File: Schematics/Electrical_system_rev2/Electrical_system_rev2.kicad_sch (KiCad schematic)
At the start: 38 parts, among them J1 DTM04-12PA-L012, J10 DTM06-12SA, J13 DTM06-12SA, J14 DTM04-12PA-L012, J17 DTM06-12SA, J18 DTM04-12PA-L012, J19 211102-1, J2 DTM06-12SA, J20 206429-1, J21 211102-1, J22 206429-1, J23 206429-1, J24 211102-1, J7 UPCR012ALS1, J8 UPCP012ALS2, SW3 2843011, SW4 2843011, SW5 84-5330.0020, SW7 84-5330.0020

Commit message: fixed checkbox
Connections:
- net SDC_to_TSMS: no longer J23.4 (Pin_4)
- net SDC_to_dash: now also J23.4 (Pin_4); no longer J23.2 (Pin_2)
- net at J24.2 (Pin_2): no longer SW7.1 (A)
- net at J24.3 (Pin_3): no longer SW5.1 (A)
- net at J2.9 (Pin_9): no longer J2.9 (Pin_9)
- net Checkbox/Reset_out: no longer names the net of J1.12 (Pin_12)
- net Checkbox/SDC1: no longer names the net of J1.9 (Pin_9)
- net SDC_from_dash: no longer names the net of J23.3 (Pin_3)
- new net: SW5.1 (A), SW7.1 (A)
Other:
- sheet Checkbox ports: added none; removed Reset_out, SDC1
- sheet Dashboard ports: added SDC_to_TSMS; removed SDC_from_dash

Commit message: SDC
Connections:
- net SDC_to_SDB: now also J14.2 (Pin_2); no longer J14.4 (Pin_4), SW4.1 (A)
- net Checkbox/SDC3: now reaches J13.2 (Pin_2)
- net Checkbox/GLV_switch renamed Checkbox/GLVMS_in
- new net: J14.4 (Pin_4), SW4.1 (A)
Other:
- sheet Checkbox ports: added GLVMS_in, Reset_out, SDC3, fan1-, fan2-, pump2-; removed GLV_switch
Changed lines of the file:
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@@
 	)
 	(junction
-		(at 288.29 210.82)
-		(diameter 0)
-		(color 0 0 0 0)
-	)
-	(junction
 		(at 300.99 210.82)
 		(diameter 0)
@@
 		)
 	)
+	(wire
+		(pts
+			(xy 306.07 170.18) (xy 306.07 175.26)
+		)
+		(stroke
+			(width 0)
+			(type default)
+		)
+	)
 	(bus
 		(pts
@@
 		)
 	)
-	(wire
+	(bus
 		(pts
-			(xy 284.48 210.82) (xy 288.29 210.82)
+			(xy 313.69 151.13) (xy 316.23 151.13)
 		)
 		(stroke
@@
 		)
 	)
-	(bus
+	(wire
 		(pts
-			(xy 313.69 151.13) (xy 316.23 151.13)
+			(xy 289.56 173.99) (xy 289.56 162.56)
 		)
 		(stroke
 			(width 0)
 			(type default)
+			(color 204 102 0 1)
 		)
 	)
 	(wire
 		(pts
-			(xy 289.56 173.99) (xy 289.56 162.56)
+			(xy 306.07 148.59) (xy 306.07 154.94)
 		)
 		(stroke
 			(width 0)
 			(type default)
-			(color 204 102 0 1)
 		)
 	)
@@
 		)
 	)
-	(global_label "SIN1"
-		(shape bidirectional)
-		(at 271.78 323.85 270)
+	(global_label "SDC_to_SDB"
+		(shape output)
+		(at 306.07 175.26 270)
 		(fields_autoplaced yes)
 		(effects
@@
 		)
 		(property "Intersheetrefs" "${INTERSHEET_REFS}"
-			(at 271.78 332.2214 90)
+			(at 306.07 189.5541 90)
 			(effects
 				(font
@@
 		)
 	)
-	(global_label "TEMP_sig"
+	(global_label "SIN1"
 		(shape bidirectional)
-		(at 259.08 323.85 270)
+		(at 271.78 323.85 270)
 		(fields_autoplaced yes)
 		(effects
@@
 		)
 		(property "Intersheetrefs" "${INTERSHEET_REFS}"
-			(at 259.08 336.4546 90)
+			(at 271.78 332.2214 90)
 			(effects
 				(font
@@
 		)
 	)
-	(global_label "COS2"
+	(global_label "TEMP_sig"
 		(shape bidirectional)
-		(at 394.97 299.72 0)
+		(at 259.08 323.85 270)
 		(fields_autoplaced yes)
 		(effects
@@
 				(size 1.27 1.27)
 			)
-			(justify left)
+			(justify right)
 		)
 		(property "Intersheetrefs" "${INTERSHEET_REFS}"
-			(at 404.0066 299.72 0)
+			(at 259.08 336.4546 90)
 			(effects
 				(font
 					(size 1.27 1.27)
 				)
-				(justify left)
+				(justify right)
 				(hide yes)
 			)
 		)
 	)
-	(global_label "SDC_to_SDB"
-		(shape input)
-		(at 360.68 233.68 90)
+	(global_label "COS2"
+		(shape bidirectional)
+		(at 394.97 299.72 0)
 		(fields_autoplaced yes)
 		(effects
@@
 		)
 		(property "Intersheetrefs" "${INTERSHEET_REFS}"
-			(at 360.68 219.3859 90)
+			(at 404.0066 299.72 0)
 			(effects
 				(font
@@
 	)
 	(global_label "SDC_to_SDB"
-		(shape output)
-		(at 284.48 210.82 180)
+		(shape input)
+		(at 360.68 233.68 90)
 		(fields_autoplaced yes)
 		(effects
@@
 				(size 1.27 1.27)
 			)
-			(justify right)
+			(justify left)
 		)
 		(property "Intersheetrefs" "${INTERSHEET_REFS}"
-			(at 270.1859 210.82 0)
+			(at 360.68 219.3859 90)
 			(effects
 				(font
 					(size 1.27 1.27)
 				)
-				(justify right)
+				(justify left)
 				(hide yes)
 			)
@@
 			)
 		)
-		(pin "GLV_switch" input
+		(pin "GLVMS_in" input
 			(at 311.15 148.59 270)
 			(effects
@@
 			(effects
 				(font
+					(size 1.27 1.27)
+				)
+				(justify left)
+			)
+		)
+		(pin "SDC3" input
+			(at 306.07 148.59 270)
+			(effects
+				(font
+					(size 1.27 1.27)
+				)
+				(justify left)
+			)
+		)
+		(pin "fan1-" input
+			(at 288.29 148.59 270)
+			(effects
+				(font
+					(size 1.27 1.27)
+				)
+				(justify left)
+			)
+		)
+		(pin "fan2-" input
+			(at 284.48 148.59 270)
+			(effects
+				(font
+					(size 1.27 1.27)
+				)
+				(justify left)
+			)
+		)
+		(pin "Reset_out" input
+			(at 299.72 148.59 270)
+			(effects
+				(font
+					(size 1.27 1.27)
+				)
+				(justify left)
+			)
+		)
+		(pin "pump2-" input
+			(at 295.91 148.59 270)
+			(effects
+				(font

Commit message: updating of electrical system
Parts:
- removed J7 (x2): UPCR012ALS1, symbol Connector:Conn_01x04_Socket
- removed J8 (x2): UPCP012ALS2, symbol Connector:Conn_01x04_Pin
- added J25: DTM04-12PA-L012, symbol Connector:Conn_01x12_Socket
- added J26: DTM06-12SA, symbol Connector:Conn_01x12_Pin
- added J27: UPCP012ALS2, symbol Connector:Conn_01x04_Pin
- added J28: UPCR012ALS1, symbol Connector:Conn_01x04_Socket
- added J29: 33482-4001, symbol Connector:Conn_01x04_Socket
- added SW10: 2843011, symbol Switch:SW_SPST
- added U18: ~, symbol FSAE:Emeter
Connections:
- net Checkbox/GLV+_fan2 is gone; now on an unnamed net: J17.2 (Pin_2)
- net Checkbox/HV+: now also J21.1 (Pin_1)
- net Checkbox/HV-: now also J21.2 (Pin_2)
- net SDC_to_TSMS: now also J26.1 (Pin_1); no longer SW3.1 (A)
- net at J8.3 (Pin_3): now also B1. (Battery-)
- net at J8.4 (Pin_4): now also J27.3 (Pin_3)
- net at B1. (Battery-): now also J27.4 (Pin_4)
- net at J14.1 (Pin_1): now also SW10.2 (B); no longer D4.2 (A)
- net at SW3.2 (B): now also J25.1 (Pin_1); no longer J14.3 (Pin_3)
- net at J14.4 (Pin_4): now also J26.3 (Pin_3); no longer SW4.1 (A)
- net TSMS_to_accum: now reaches J2.9 (Pin_9)
- net TSMS_to_accum: now also J14.3 (Pin_3), J26.2 (Pin_2)
- net HV+: now reaches R3.2, TP2.1
- net HV+: now also U18. (VSENSE)
- net Checkbox/GLV+_fan1: no longer names the net of J17.1 (Pin_1)
- net Checkbox/GLV+_pump1: no longer names the net of J17.5 (Pin_5), J17.6 (Pin_6)
- net Checkbox/GLV+_pump2: no longer names the net of J17.3 (Pin_3), J17.4 (Pin_4)
- net Checkbox/accum_motor+: no longer names the net of J17.7 (Pin_7)
- net Checkbox/accum_motor-: no longer names the net of J17.8 (Pin_8)
- net Checkbox/temp1_motor+: no longer names the net of J17.11 (Pin_11)
- net Checkbox/temp1_motor-: no longer names the net of J17.12 (Pin_12)
- net Checkbox/temp2_motor+: no longer names the net of J17.9 (Pin_9)
- net Checkbox/temp2_motor-: no longer names the net of J17.10 (Pin_10)
- new net: J25.3 (Pin_3), SW4.2 (B)
- new net: J14.5 (Pin_5), J26.4 (Pin_4)
- new net: J29.1 (Pin_1), U18.4 (CANH)
- new net: J29.2 (Pin_2), U18.3 (CANL)
- new net: D4.2 (A), SW10.1 (A)
- new net: J28.3 (Pin_3), U18. (VSENSE)
- new net: J28.4 (Pin_4), U18. (VSENSE)
- new net GLVMS: J25.4 (Pin_4), J29.4 (Pin_4), SW4.1 (A), U18.1 (GLV+)
- new net GND: J25.5 (Pin_5), J29.3 (Pin_3), TP3.1, U18.2 (GLV-)
- new net GNDPWR: J26.5 (Pin_5)
- new net TSMS: J28.1 (Pin_1), SW3.1 (A)
- new net TSMS_out: J25.2 (Pin_2), J28.2 (Pin_2)
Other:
- sheet Checkbox ports: added GLV+_fan, GLV+_pump_accum, GLV+_pump_motor; removed GLV+_fan1, GLV+_fan2, GLV+_pump1, GLV+_pump2, HV+_to_motor, HV-_to_motor, accum_motor+, accum_motor-, fan1-, fan2-, temp1_motor+, temp1_motor-, temp2_motor+, temp2_motor-
- sheet Cooling ports: added Fans-, GLV+_fan, GLV+_pump_accum, GLV+_pump_motor, Pump_accum-, pump_motor_pwm, temp1+, temp1-, temp2+, temp2-; removed GLV+_pump1, fan1+, fan2+, pump1_control, pump2_control, temp1_motor+, temp1_motor-, temp2_motor+, temp2_motor-
- sheet Dashboard ports: added Fans-, Pump_accum-, temp1+, temp1-, temp2+, temp2-, temp_accum+, temp_accum-; removed Reset_from_dash
- note added: "Brake switch"
- note added: "Download Connector"
- note added: "GND while charging, floating when not"
- note added: "HV High Current"
- note added: "HV Low Current"
- note added: "HVD"
- note added: "LV"
- note removed: "GND while charging, 12V when not"
- moved on the sheet: J19, J22, R2, R3, TP1, TP2

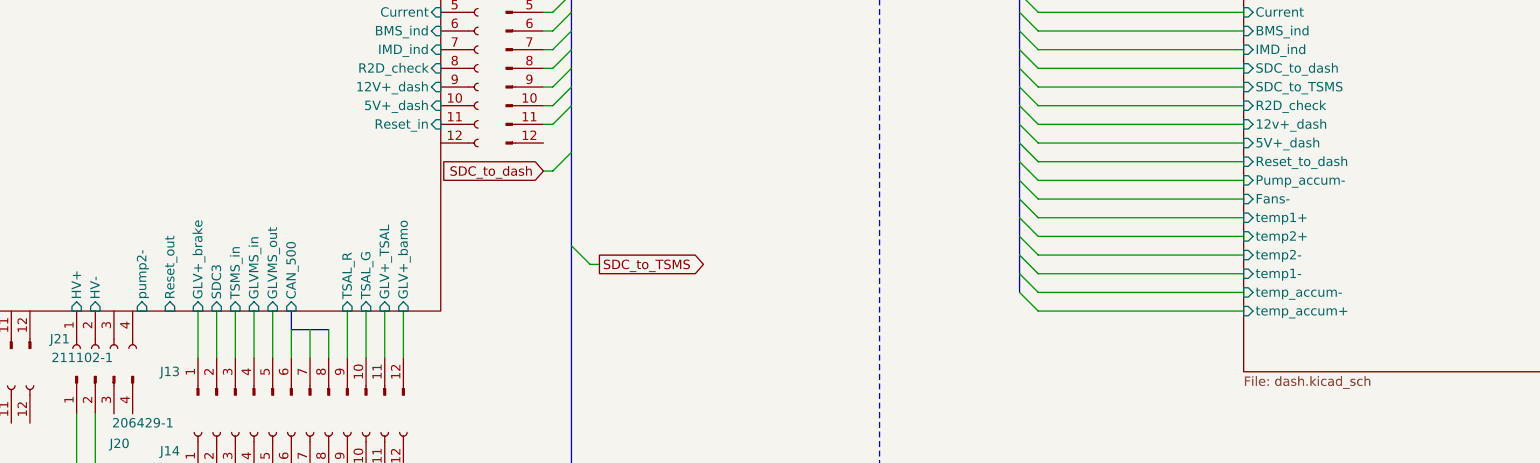
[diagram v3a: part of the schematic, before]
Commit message: fixed reset switch
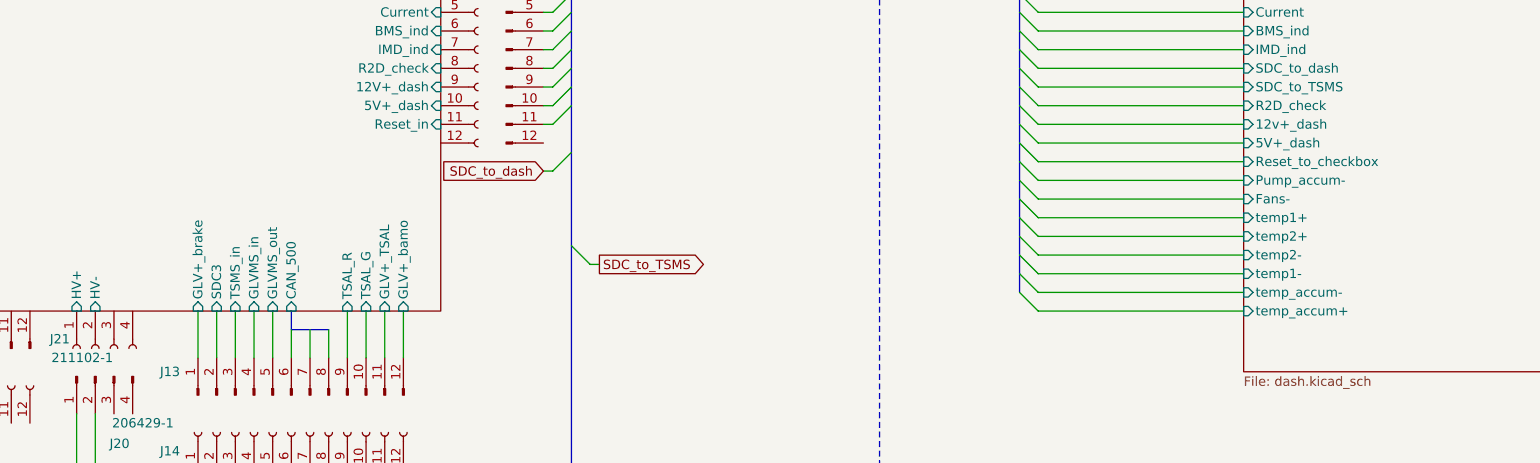
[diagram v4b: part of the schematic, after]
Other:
- sheet Checkbox ports: added none; removed Reset_out, pump2-
- sheet Dashboard ports: added Reset_to_checkbox; removed Reset_to_dash
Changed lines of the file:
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@@
-			)
-		)
-		(pin "Reset_out" input
-			(at 299.72 148.59 270)
-			(effects
-				(font
-					(size 1.27 1.27)
-				)
-				(justify left)
-			)
-		)
-		(pin "pump2-" input
-			(at 295.91 148.59 270)
-			(effects
-				(font
-					(size 1.27 1.27)
-				)
-				(justify left)
 			)
 		)
@@
 			)
 		)
-		(pin "Reset_to_dash" input
+		(pin "Reset_to_checkbox" input
 			(at 445.77 128.27 180)
 			(effects

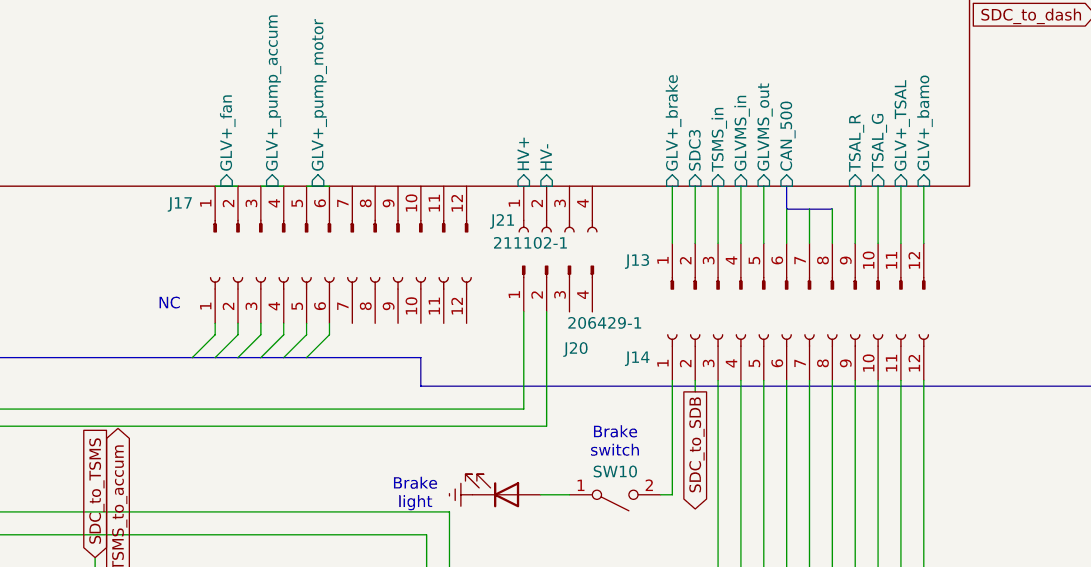
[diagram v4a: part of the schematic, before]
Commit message: swapped male and female connectors
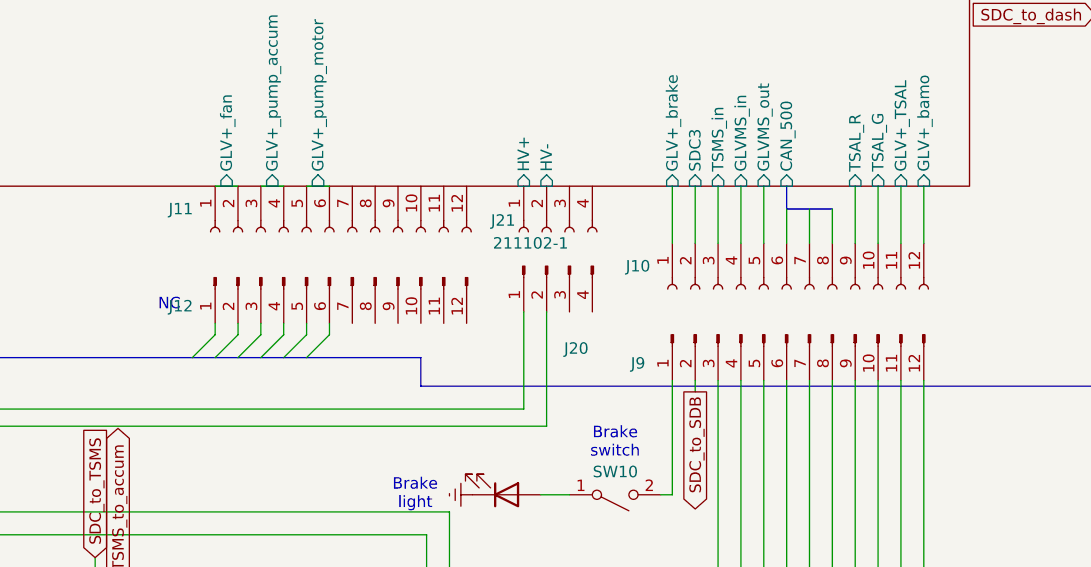
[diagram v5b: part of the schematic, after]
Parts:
- removed J13, J17: DTM06-12SA, symbol Connector:Conn_01x12_Pin
- removed J14, J18: DTM04-12PA-L012, symbol Connector:Conn_01x12_Socket
- added J10, J11: DTM04-12PA-L012, symbol Connector:Conn_01x12_Socket
- added J12, J9: DTM06-12SA, symbol Connector:Conn_01x12_Pin
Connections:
- net Checkbox/GLV+_TSAL: now also J10.11 (Pin_11)
- net Checkbox/GLV+_bamo: now also J10.12 (Pin_12)
- net Checkbox/GLV+_brake: now also J10.1 (Pin_1)
- net Checkbox/GLVMS_in: now also J10.4 (Pin_4)
- net Checkbox/GLVMS_out: now also J10.5 (Pin_5)
- net Checkbox/SDC3: now also J10.2 (Pin_2)
- net Checkbox/TSAL_G: now also J10.10 (Pin_10)
- net Checkbox/TSAL_R: now also J10.9 (Pin_9)
- net Checkbox/TSMS_in: now also J10.3 (Pin_3)
- net SDC_to_SDB: now also J9.2 (Pin_2)
- net TSMS_to_accum: now also J9.3 (Pin_3)
- net at D2.1 (K): now also J9.10 (Pin_10)
- net at D2.2 (A): now also J9.11 (Pin_11)
- net at SW10.2 (B): now also J9.1 (Pin_1)
- net at J26.3 (Pin_3): now also J9.4 (Pin_4)
- net at J26.4 (Pin_4): now also J9.5 (Pin_5)
- net at D1.2 (A): now also J9.9 (Pin_9)
- new net: J11.1 (Pin_1), J11.2 (Pin_2)
- new net: J11.3 (Pin_3), J11.4 (Pin_4)
- new net: J11.5 (Pin_5), J11.6 (Pin_6)

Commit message: updated numberings
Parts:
- renumbered D4 to D1, D1 to D3, J10 to J13, J9 to J14, J22 to J17, J26 to J18, J27 to J19, J19 to J20, J25 to J21, J28 to J22, J29 to J23, J23 to J24, J24 to J25, J11 to J7, J21 to J8, J20 to J9, R2 to R1, R3 to R2, SW10 to SW1, SW3 to SW2, SW4 to SW3, SW7 to SW4, TP2 to TP1, TP1 to TP2, U18 to U1

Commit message: small edits
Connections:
- net Accumulator/HV+: now also J7.3 (Pin_3)
- net Accumulator/HV-: now also J7.4 (Pin_4)
- net Accumulator/IL1: now also J7.1 (Pin_1)
- net Accumulator/IL2: now also J7.2 (Pin_2)
- net Checkbox/GLV+_fan: now also J7.1 (Pin_1), J7.2 (Pin_2)
- net Checkbox/GLV+_pump_accum: now also J7.3 (Pin_3), J7.4 (Pin_4)
- net Checkbox/GLV+_pump_motor: now also J7.5 (Pin_5), J7.6 (Pin_6)
- net Checkbox/GLVMS_in: now also J7.10 (Pin_10), J7.11 (Pin_11); no longer J13.4 (Pin_4)
- net Checkbox/GLVMS_out: now also J7.8 (Pin_8), J7.9 (Pin_9); no longer J13.5 (Pin_5)
- net Checkbox/TSMS_in: now also J7.12 (Pin_12); no longer J13.3 (Pin_3)
- net GLVMS: now also J21.5 (Pin_5), J21.6 (Pin_6); no longer J21.4 (Pin_4)
- net GND: now also J21.7 (Pin_7); no longer J21.5 (Pin_5)
- net GNDPWR: now also J18.7 (Pin_7); no longer J18.5 (Pin_5)
- net TSMS_to_accum: now also J12.12 (Pin_12); no longer J14.3 (Pin_3)
- net at J21.3 (Pin_3), SW3.2 (B): now also J21.4 (Pin_4)
- net at B1. (Battery-): no longer J8.3 (Pin_3)
- net at J19.4 (Pin_4): no longer B1. (Battery-)
- net at J19.1 (Pin_1): now also J19.2 (Pin_2)
- net at J18.3 (Pin_3): now also J12.8 (Pin_8), J12.9 (Pin_9), J18.4 (Pin_4); no longer J14.4 (Pin_4)
- net at J14.5 (Pin_5): no longer J18.4 (Pin_4)
- net at J18.6 (Pin_6): now also J12.10 (Pin_10), J12.11 (Pin_11), J18.5 (Pin_5)
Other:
- moved on the sheet: J17, J18, J19, J20, J21, J22, SW2, TP3, U1
